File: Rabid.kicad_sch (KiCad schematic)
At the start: 223 parts, among them J1 USB Connector, J3 GPIO Debug Header, SW1 Esc, SW10 A, SW100 Unused, SW101 Unused, SW102 →, SW103 BootSel Switch, SW104 Reset Switch, SW11 Z, SW12 LMeta, SW13 F1, SW14 2, SW15 W, SW16 S, SW17 X, SW18 LAlt, SW19 F2, SW2 Tilde, SW20 3, SW21 E, SW22 D, SW23 C, SW24 Unused, SW25 F3, SW26 4, SW27 R, SW28 F, SW29 V, SW3 Tab, SW30 Unused, SW31 F4, SW32 5, SW33 T, SW34 G, SW35 B, SW36 Unused, SW37 F5, SW38 6, SW39 Y, SW4 CapsLk, SW40 H, SW41 N, SW42 Space, SW43 F6, SW44 7, SW45 U, SW46 J, SW47 M, SW48 Unused, SW49 F7, SW5 LShift, SW50 8, SW51 I, SW52 K, SW53 ,, SW54 Unused, SW55 F8, SW56 9, SW57 O, SW58 L, SW59 ., SW6 LCtrl, SW60 Unused, SW61 F9, SW62 0, SW63 P, SW64 ;, SW65 /, SW66 AltGr, SW67 F10, SW68 -, SW69 [, SW7 Unused, SW70 ", SW71 RShift, SW72 RMeta, SW73 F11, SW74 =, SW75 ]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

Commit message: Change Filco hole from 4mm to 5mm.
 - Rename FnLock to MetaLock.
 - Minor silkscreen changes.
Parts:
- D104: value CapsTopLED -> CapsLock
- D106: value ScrollTopLED -> ScrollLock
- D108: value FnTopLED -> MetaLock
- H3: value MountingHole_4mm -> MountingHole_5mm; footprint RabidKeyboard:MountingHole_4mm -> RabidKeyboard:MountingHole_5mm
- SW103: value BootSel Switch -> BootSel
- SW104: value Reset Switch -> Reset
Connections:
- net FnLED renamed MetaLED
- net FnLED_GPIO renamed MetaLED_GPIO
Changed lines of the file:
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@@
     (stroke (width 0) (type default) (color 0 0 0 0))
   )
-  (label "FnLED" (at 256.54 34.29 0)
+  (label "MetaLED" (at 256.54 34.29 0)
     (effects (font (size 1.27 1.27)) (justify left bottom))
   )
@@
     (effects (font (size 1.27 1.27)) (justify left bottom))
   )
-  (label "FnLED" (at 158.75 232.41 0)
+  (label "MetaLED" (at 158.75 232.41 0)
     (effects (font (size 1.27 1.27)) (justify left bottom))
   )
@@
     (effects (font (size 1.27 1.27)) (justify right bottom))
   )
-  (label "FnLED_GPIO" (at 107.95 254 0)
+  (label "MetaLED_GPIO" (at 107.95 254 0)
     (effects (font (size 1.27 1.27)) (justify left bottom))
   )
@@
     (effects (font (size 1.27 1.27)) (justify right bottom))
   )
-  (label "FnLED_GPIO" (at 147.32 237.49 180)
+  (label "MetaLED_GPIO" (at 147.32 237.49 180)
     (effects (font (size 1.27 1.27)) (justify right bottom))
   )
@@
     (in_bom yes) (on_board yes)
     (property "Reference" "D104" (id 0) (at 167.64 254 0))
-    (property "Value" "CapsTopLED" (id 1) (at 167.64 259.08 0))
+    (property "Value" "CapsLock" (id 1) (at 167.64 259.08 0))
     (property "Footprint" "LED_THT:LED_D3.0mm" (id 2) (at 167.64 256.54 0)
       (effects (font (size 1.27 1.27)) hide)
@@
       (effects (font (size 1.27 1.27)) (justify left))
     )
-    (property "Value" "MountingHole_4mm" (id 1) (at 252.73 275.5899 0)
+    (property "Value" "MountingHole_5mm" (id 1) (at 252.73 275.5899 0)
       (effects (font (size 1.27 1.27)) (justify left))
     )
-    (property "Footprint" "RabidKeyboard:MountingHole_4mm" (id 2) (at 250.19 274.32 0)
+    (property "Footprint" "RabidKeyboard:MountingHole_5mm" (id 2) (at 250.19 274.32 0)
       (effects (font (size 1.27 1.27)) hide)
     )
@@
     (in_bom yes) (on_board yes) (fields_autoplaced)
     (property "Reference" "SW104" (id 0) (at 33.02 245.11 0))
-    (property "Value" "Reset Switch" (id 1) (at 33.02 247.65 0))
+    (property "Value" "Reset" (id 1) (at 33.02 247.65 0))
     (property "Footprint" "Button_Switch_THT:SW_PUSH_6mm" (id 2) (at 33.02 247.65 0)
       (effects (font (size 1.27 1.27)) hide)
@@
     (in_bom yes) (on_board yes)
     (property "Reference" "D108" (id 0) (at 167.64 234.95 0))
-    (property "Value" "FnTopLED" (id 1) (at 167.64 240.03 0))
+    (property "Value" "MetaLock" (id 1) (at 167.64 240.03 0))
     (property "Footprint" "LED_THT:LED_D3.0mm" (id 2) (at 167.64 237.49 0)
       (effects (font (size 1.27 1.27)) hide)
@@
     (in_bom yes) (on_board yes)
     (property "Reference" "SW103" (id 0) (at 33.02 224.79 0))
-    (property "Value" "BootSel Switch" (id 1) (at 33.02 227.33 0))
+    (property "Value" "BootSel" (id 1) (at 33.02 227.33 0))
     (property "Footprint" "Button_Switch_THT:SW_PUSH_6mm" (id 2) (at 33.02 227.33 0)
       (effects (font (size 1.27 1.27)) hide)
@@
     (in_bom yes) (on_board yes)
     (property "Reference" "D106" (id 0) (at 167.64 215.9 0))
-    (property "Value" "ScrollTopLED" (id 1) (at 167.64 220.98 0))
+    (property "Value" "ScrollLock" (id 1) (at 167.64 220.98 0))
     (property "Footprint" "LED_THT:LED_D3.0mm" (id 2) (at 167.64 218.44 0)
       (effects (font (size 1.27 1.27)) hide)
@@
     )
     (path "/013f1d10-abd8-4150-895c-ca8640632826"
-      (reference "D104") (unit 1) (value "CapsTopLED") (footprint "LED_THT:LED_D3.0mm")
+      (reference "D104") (unit 1) (value "CapsLock") (footprint "LED_THT:LED_D3.0mm")
     )
     (path "/f2c2e18c-527d-412e-8b29-fe36c22fe3e6"
-      (reference "D106") (unit 1) (value "ScrollTopLED") (footprint "LED_THT:LED_D3.0mm")
+      (reference "D106") (unit 1) (value "ScrollLock") (footprint "LED_THT:LED_D3.0mm")
     )
     (path "/c8391114-3696-47a3-8a1e-475677d62fda"
-      (reference "D108") (unit 1) (value "FnTopLED") (footprint "LED_THT:LED_D3.0mm")
+      (reference "D108") (unit 1) (value "MetaLock") (footprint "LED_THT:LED_D3.0mm")
     )
     (path "/7ab71991-2b35-4dfe-a3d1-e1d6a93c8aa2"
@@
     )
     (path "/18a8f0d3-5ac8-4d2b-aaf1-8fd815948e6a"
-      (reference "H3") (unit 1) (value "MountingHole_4mm") (footprint "RabidKeyboard:MountingHole_4mm")
+      (reference "H3") (unit 1) (value "MountingHole_5mm") (footprint "RabidKeyboard:MountingHole_5mm")
     )
     (path "/23a84009-b94e-4473-821b-756b9ff8be21"
@@
     )
     (path "/cf26448c-5f86-443a-813f-8205ab4f6600"
-      (reference "SW103") (unit 1) (value "BootSel Switch") (footprint "Button_Switch_THT:SW_PUSH_6mm")
+      (reference "SW103") (unit 1) (value "BootSel") (footprint "Button_Switch_THT:SW_PUSH_6mm")
     )
     (path "/6df29cc0-92ba-4b02-9bf3-89ee5f38d720"
-      (reference "SW104") (unit 1) (value "Reset Switch") (footprint "Button_Switch_THT:SW_PUSH_6mm")
+      (reference "SW104") (unit 1) (value "Reset") (footprint "Button_Switch_THT:SW_PUSH_6mm")
     )
     (path "/192f83a9-3726-4136-83ac-7fa10874c246"

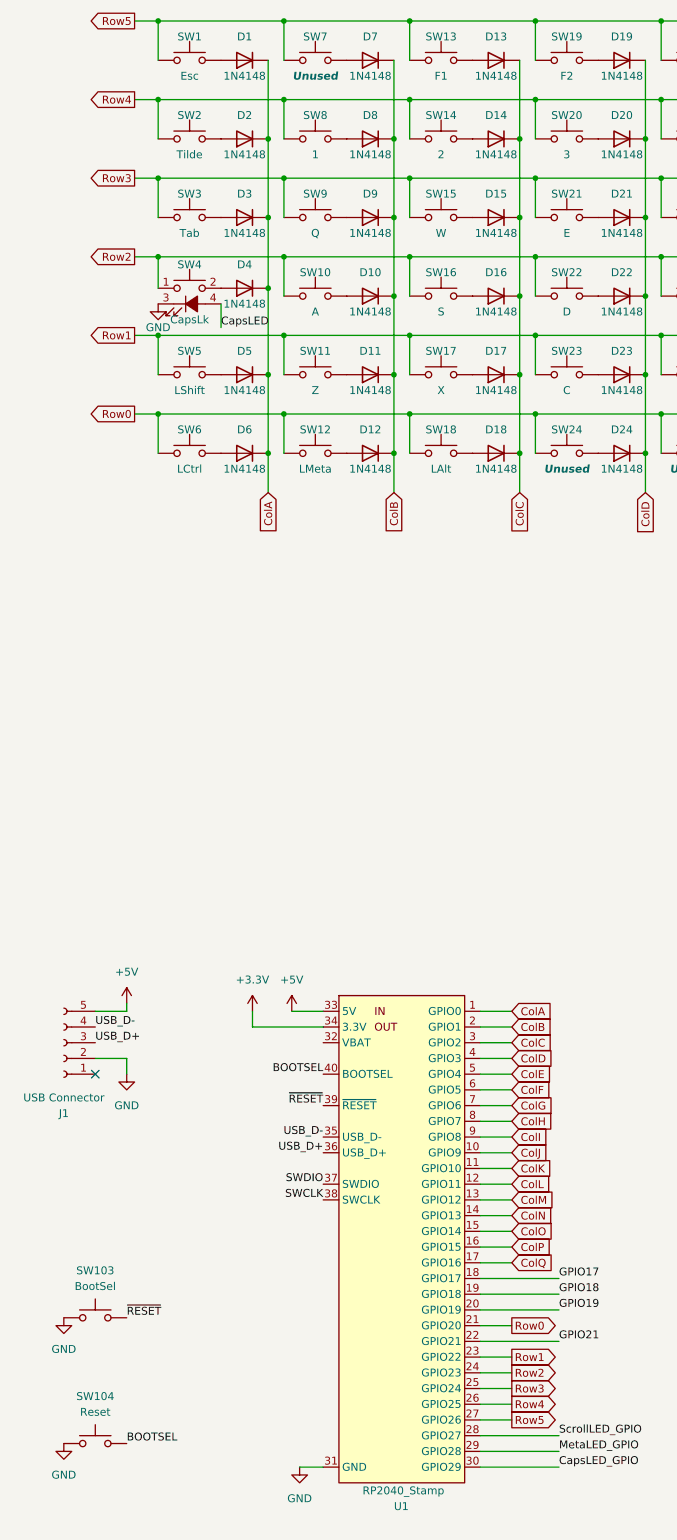
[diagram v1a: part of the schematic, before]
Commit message: Reverse direction of row pins to match firmware.
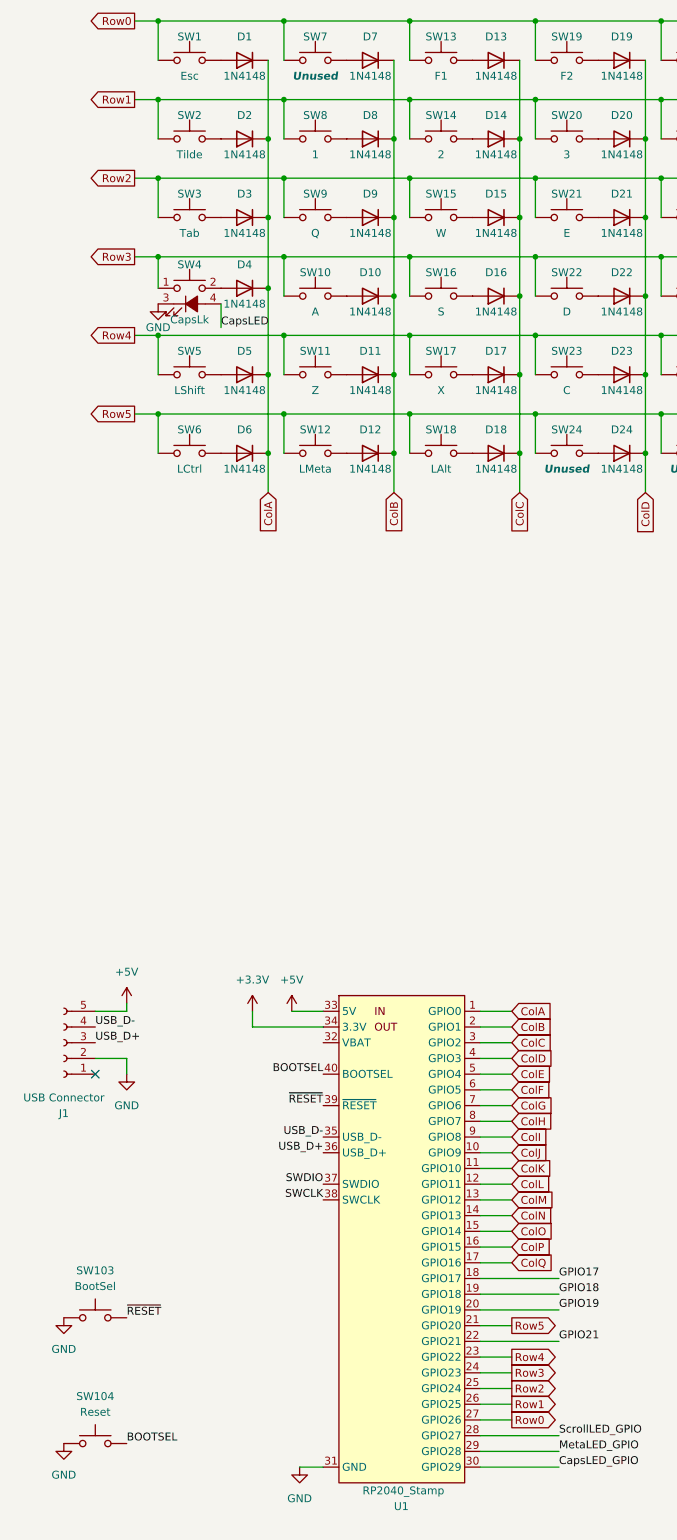
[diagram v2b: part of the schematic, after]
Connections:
- net Row0: now also SW1.1, SW13.1, SW19.1, SW25.1, SW31.1, SW37.1, SW43.1, SW49.1, SW55.1, SW61.1, SW67.1, SW7.1, SW73.1, SW79.1, SW85.1, SW91.1, SW97.1, U1.27 (GPIO26); no longer SW102.1, SW12.1, SW18.1, SW24.1, SW30.1, SW36.1, SW42.1, SW48.1, SW54.1, SW6.1, SW60.1, SW66.1, SW72.1, SW78.1, SW84.1, SW90.1, SW96.1, U1.21 (GPIO20)
- net Row1: now also SW14.1, SW2.1, SW20.1, SW26.1, SW32.1, SW38.1, SW44.1, SW50.1, SW56.1, SW62.1, SW68.1, SW74.1, SW8.1, SW80.1, SW86.1, SW92.1, SW98.1, U1.26 (GPIO25); no longer SW101.1, SW11.1, SW17.1, SW23.1, SW29.1, SW35.1, SW41.1, SW47.1, SW5.1, SW53.1, SW59.1, SW65.1, SW71.1, SW77.1, SW83.1, SW89.1, SW95.1, U1.23 (GPIO22)
- net Row2: now also SW15.1, SW21.1, SW27.1, SW3.1, SW33.1, SW39.1, SW45.1, SW51.1, SW57.1, SW63.1, SW69.1, SW75.1, SW81.1, SW87.1, SW9.1, SW93.1, SW99.1, U1.25 (GPIO24); no longer SW10.1, SW100.1, SW16.1, SW22.1, SW28.1, SW34.1, SW4.1, SW40.1, SW46.1, SW52.1, SW58.1, SW64.1, SW70.1, SW76.1, SW82.1, SW88.1, SW94.1, U1.24 (GPIO23)
- net Row3: now also SW10.1, SW100.1, SW16.1, SW22.1, SW28.1, SW34.1, SW4.1, SW40.1, SW46.1, SW52.1, SW58.1, SW64.1, SW70.1, SW76.1, SW82.1, SW88.1, SW94.1, U1.24 (GPIO23); no longer SW15.1, SW21.1, SW27.1, SW3.1, SW33.1, SW39.1, SW45.1, SW51.1, SW57.1, SW63.1, SW69.1, SW75.1, SW81.1, SW87.1, SW9.1, SW93.1, SW99.1, U1.25 (GPIO24)
- net Row4: now also SW101.1, SW11.1, SW17.1, SW23.1, SW29.1, SW35.1, SW41.1, SW47.1, SW5.1, SW53.1, SW59.1, SW65.1, SW71.1, SW77.1, SW83.1, SW89.1, SW95.1, U1.23 (GPIO22); no longer SW14.1, SW2.1, SW20.1, SW26.1, SW32.1, SW38.1, SW44.1, SW50.1, SW56.1, SW62.1, SW68.1, SW74.1, SW8.1, SW80.1, SW86.1, SW92.1, SW98.1, U1.26 (GPIO25)
- net Row5: now also SW102.1, SW12.1, SW18.1, SW24.1, SW30.1, SW36.1, SW42.1, SW48.1, SW54.1, SW6.1, SW60.1, SW66.1, SW72.1, SW78.1, SW84.1, SW90.1, SW96.1, U1.21 (GPIO20); no longer SW1.1, SW13.1, SW19.1, SW25.1, SW31.1, SW37.1, SW43.1, SW49.1, SW55.1, SW61.1, SW67.1, SW7.1, SW73.1, SW79.1, SW85.1, SW91.1, SW97.1, U1.27 (GPIO26)
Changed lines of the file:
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@@
     )
   )
-  (global_label "Row1" (shape output) (at 39.37 73.66 180) (fields_autoplaced)
+  (global_label "Row4" (shape output) (at 39.37 73.66 180) (fields_autoplaced)
     (effects (font (size 1.27 1.27)) (justify right))
     (property "Intersheet References" "${INTERSHEET_REFS}" (id 0) (at 31.9979 73.5806 0)
@@
     )
   )
-  (global_label "Row5" (shape output) (at 39.37 22.86 180) (fields_autoplaced)
+  (global_label "Row0" (shape output) (at 39.37 22.86 180) (fields_autoplaced)
     (effects (font (size 1.27 1.27)) (justify right))
     (property "Intersheet References" "${INTERSHEET_REFS}" (id 0) (at 31.9979 22.7806 0)
@@
     )
   )
-  (global_label "Row2" (shape output) (at 39.37 60.96 180) (fields_autoplaced)
+  (global_label "Row3" (shape output) (at 39.37 60.96 180) (fields_autoplaced)
     (effects (font (size 1.27 1.27)) (justify right))
     (property "Intersheet References" "${INTERSHEET_REFS}" (id 0) (at 31.9979 60.8806 0)
@@
     )
   )
-  (global_label "Row1" (shape output) (at 100.33 238.76 0) (fields_autoplaced)
+  (global_label "Row4" (shape output) (at 100.33 238.76 0) (fields_autoplaced)
     (effects (font (size 1.27 1.27)) (justify left))
     (property "Intersheet References" "${INTERSHEET_REFS}" (id 0) (at 107.7021 238.6806 0)
-      (effects (font (size 1.27 1.27)) (justify right) hide)
+      (effects (font (size 1.27 1.27)) (justify left) hide)
     )
   )
@@
     )
   )
-  (global_label "Row4" (shape output) (at 39.37 35.56 180) (fields_autoplaced)
+  (global_label "Row1" (shape output) (at 39.37 35.56 180) (fields_autoplaced)
     (effects (font (size 1.27 1.27)) (justify right))
     (property "Intersheet References" "${INTERSHEET_REFS}" (id 0) (at 31.9979 35.4806 0)
@@
     )
   )
-  (global_label "Row5" (shape output) (at 100.33 248.92 0) (fields_autoplaced)
+  (global_label "Row0" (shape output) (at 100.33 248.92 0) (fields_autoplaced)
     (effects (font (size 1.27 1.27)) (justify left))
     (property "Intersheet References" "${INTERSHEET_REFS}" (id 0) (at 107.7021 248.8406 0)
-      (effects (font (size 1.27 1.27)) (justify right) hide)
+      (effects (font (size 1.27 1.27)) (justify left) hide)
     )
   )
@@
     )
   )
-  (global_label "Row0" (shape output) (at 100.33 233.68 0) (fields_autoplaced)
-    (effects (font (size 1.27 1.27)) (justify left))
-    (property "Intersheet References" "${INTERSHEET_REFS}" (id 0) (at 107.7021 233.7594 0)
-      (effects (font (size 1.27 1.27)) (justify right) hide)
+  (global_label "Row5" (shape output) (at 100.33 233.68 0) (fields_autoplaced)
+    (effects (font (size 1.27 1.27)) (justify left))
+    (property "Intersheet References" "${INTERSHEET_REFS}" (id 0) (at 107.7021 233.6006 0)
+      (effects (font (size 1.27 1.27)) (justify left) hide)
     )
   )
@@
     )
   )
-  (global_label "Row4" (shape output) (at 100.33 246.38 0) (fields_autoplaced)
+  (global_label "Row1" (shape output) (at 100.33 246.38 0) (fields_autoplaced)
     (effects (font (size 1.27 1.27)) (justify left))
     (property "Intersheet References" "${INTERSHEET_REFS}" (id 0) (at 107.7021 246.3006 0)
-      (effects (font (size 1.27 1.27)) (justify right) hide)
+      (effects (font (size 1.27 1.27)) (justify left) hide)
     )
   )
@@
     )
   )
-  (global_label "Row2" (shape output) (at 100.33 241.3 0) (fields_autoplaced)
+  (global_label "Row3" (shape output) (at 100.33 241.3 0) (fields_autoplaced)
     (effects (font (size 1.27 1.27)) (justify left))
     (property "Intersheet References" "${INTERSHEET_REFS}" (id 0) (at 107.7021 241.2206 0)
-      (effects (font (size 1.27 1.27)) (justify right) hide)
+      (effects (font (size 1.27 1.27)) (justify left) hide)
     )
   )
@@
     )
   )
-  (global_label "Row3" (shape output) (at 39.37 48.26 180) (fields_autoplaced)
+  (global_label "Row2" (shape output) (at 39.37 48.26 180) (fields_autoplaced)
     (effects (font (size 1.27 1.27)) (justify right))
     (property "Intersheet References" "${INTERSHEET_REFS}" (id 0) (at 31.9979 48.1806 0)
@@
     )
   )
-  (global_label "Row0" (shape output) (at 39.37 86.36 180) (fields_autoplaced)
+  (global_label "Row5" (shape output) (at 39.37 86.36 180) (fields_autoplaced)
     (effects (font (size 1.27 1.27)) (justify right))
     (property "Intersheet References" "${INTERSHEET_REFS}" (id 0) (at 31.9979 86.2806 0)
@@
     )
   )
-  (global_label "Row3" (shape output) (at 100.33 243.84 0) (fields_autoplaced)
+  (global_label "Row2" (shape output) (at 100.33 243.84 0) (fields_autoplaced)
     (effects (font (size 1.27 1.27)) (justify left))
     (property "Intersheet References" "${INTERSHEET_REFS}" (id 0) (at 107.7021 243.7606 0)
-      (effects (font (size 1.27 1.27)) (justify right) hide)
-    )
-  )
+      (effects (font (size 1.27 1.27)) (justify left) hide)
+    )
+  )
